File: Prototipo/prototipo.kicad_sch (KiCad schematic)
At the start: 13 parts, among them J1 Conn_02x12_Odd_Even

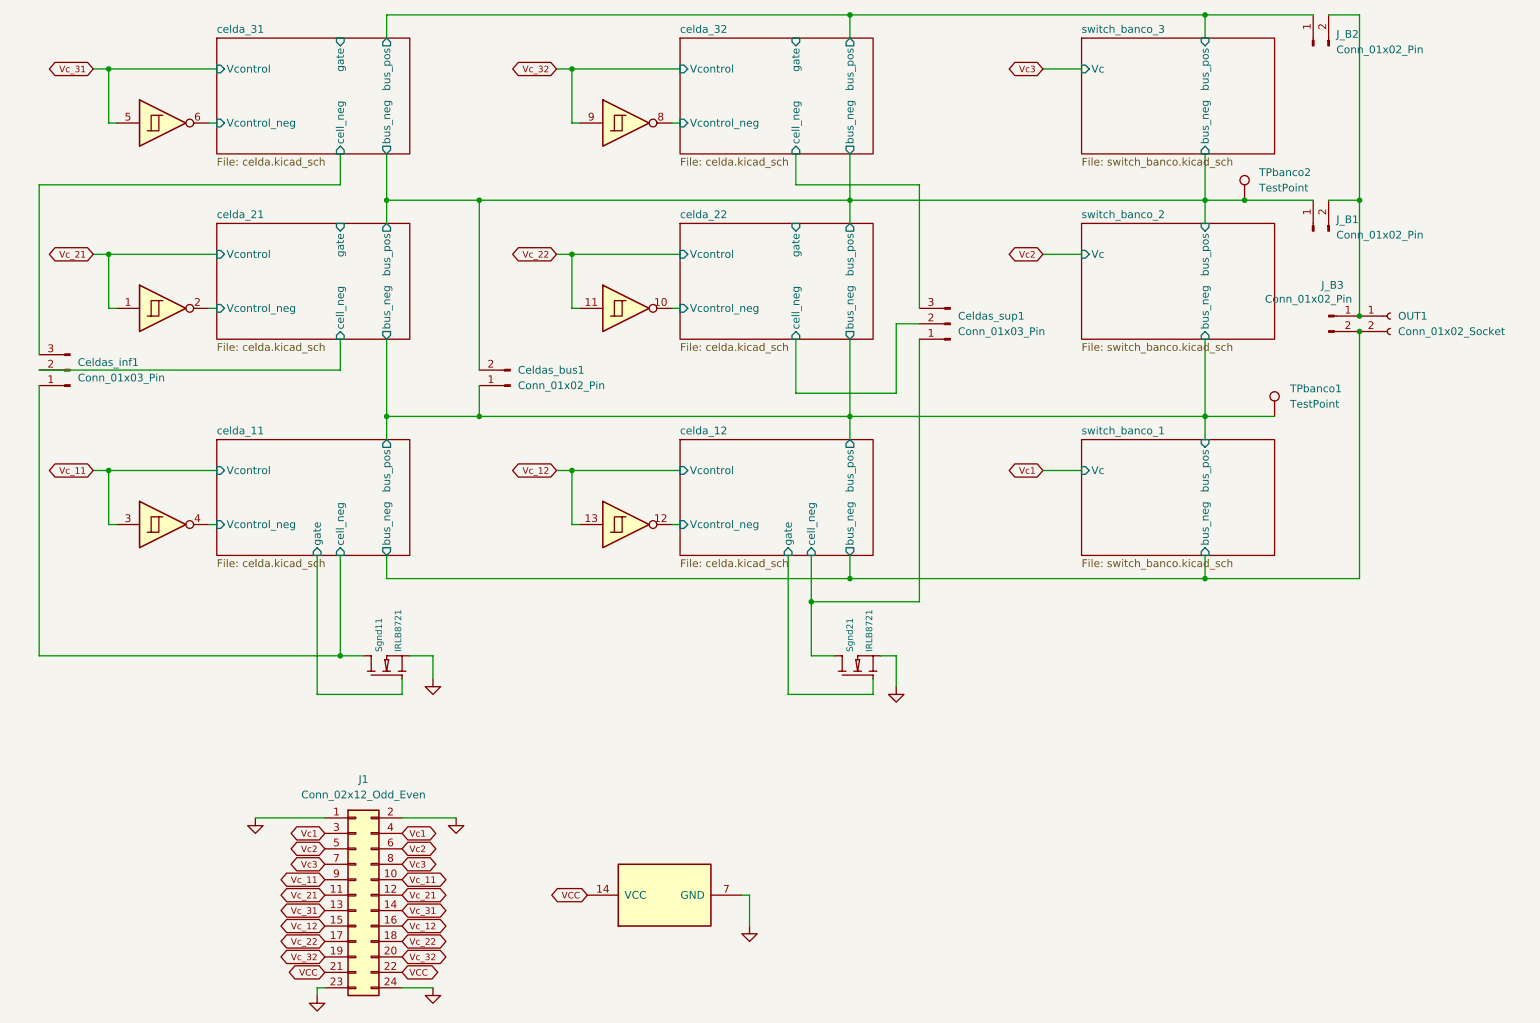
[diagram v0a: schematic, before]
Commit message: Sumo ultimos cambios hablados en reunion
agrega agujeros para tornillos, jumper para banco 1, INVERSOR CON ZOCALO, cambia el diametro de test points y vias, acomoda serigrafia, SIN WARNINGS
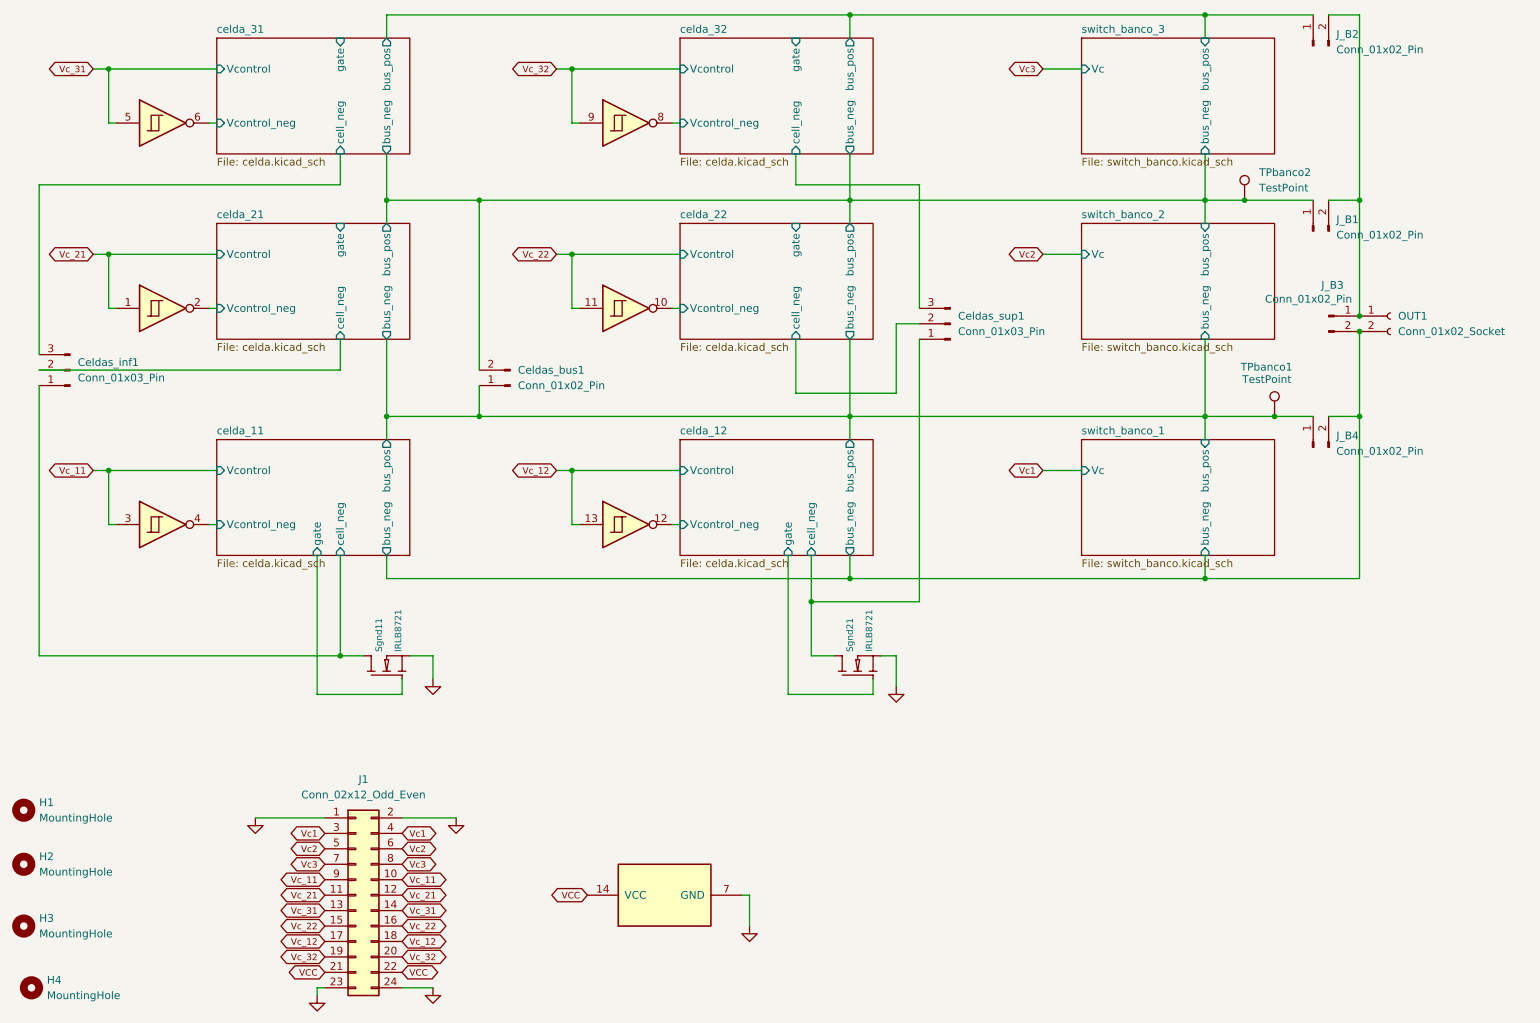
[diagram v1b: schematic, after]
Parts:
- added H1, H2, H3, H4: MountingHole, MountingHole:MountingHole_3.2mm_M3, symbol Mechanical:MountingHole
- added J_B4: Conn_01x02_Pin, Connector_PinHeader_2.54mm:PinHeader_1x02_P2.54mm_Vertical, symbol Connector:Conn_01x02_Pin
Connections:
- net Vc_12: now also J1.17 (Pin_17), J1.18 (Pin_18); no longer J1.15 (Pin_15), J1.16 (Pin_16)
- net Vc_22: now also J1.15 (Pin_15), J1.16 (Pin_16); no longer J1.17 (Pin_17), J1.18 (Pin_18)
- net celda_11/bus_neg: now also J_B4.2 (Pin_2)
- net celda_11/bus_pos: now also J_B4.1 (Pin_1)
